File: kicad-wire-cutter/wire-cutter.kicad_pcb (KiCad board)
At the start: 2 copper layers, 60.7 x 113.1 mm, 21 parts, among them J1 Conn_01x01_Socket, J3 Conn_01x01_Socket, U4 ESP32-DEVKIT-V1

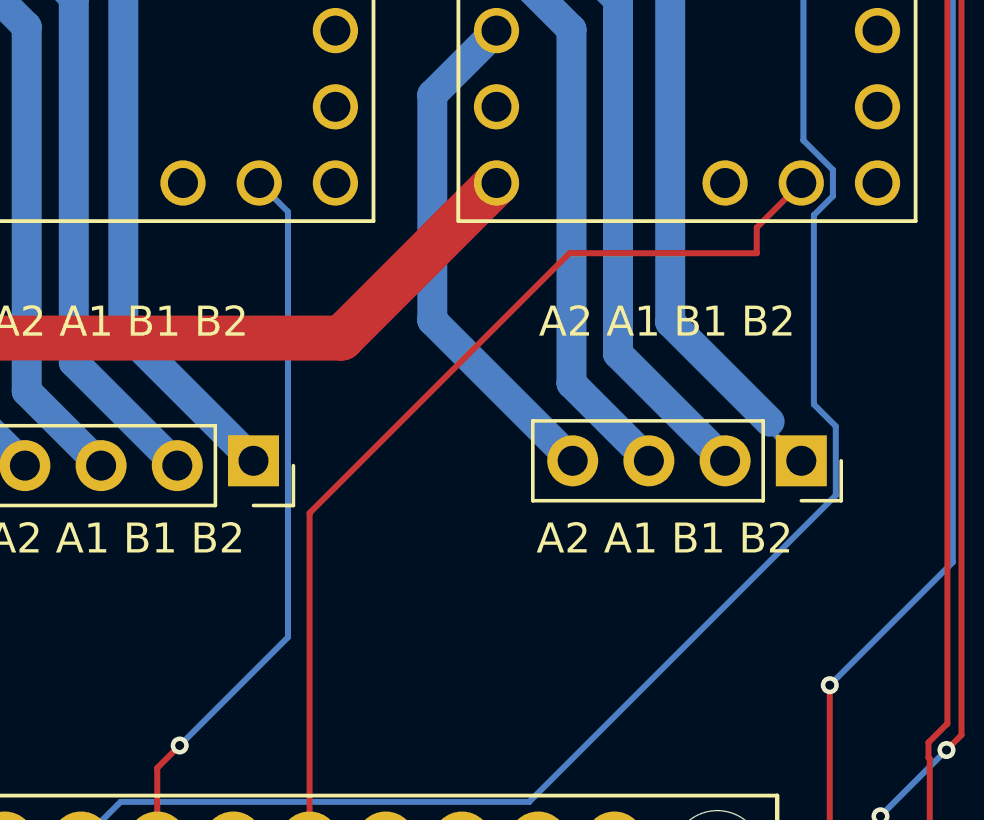
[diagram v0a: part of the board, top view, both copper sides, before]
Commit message: Finished full cut process
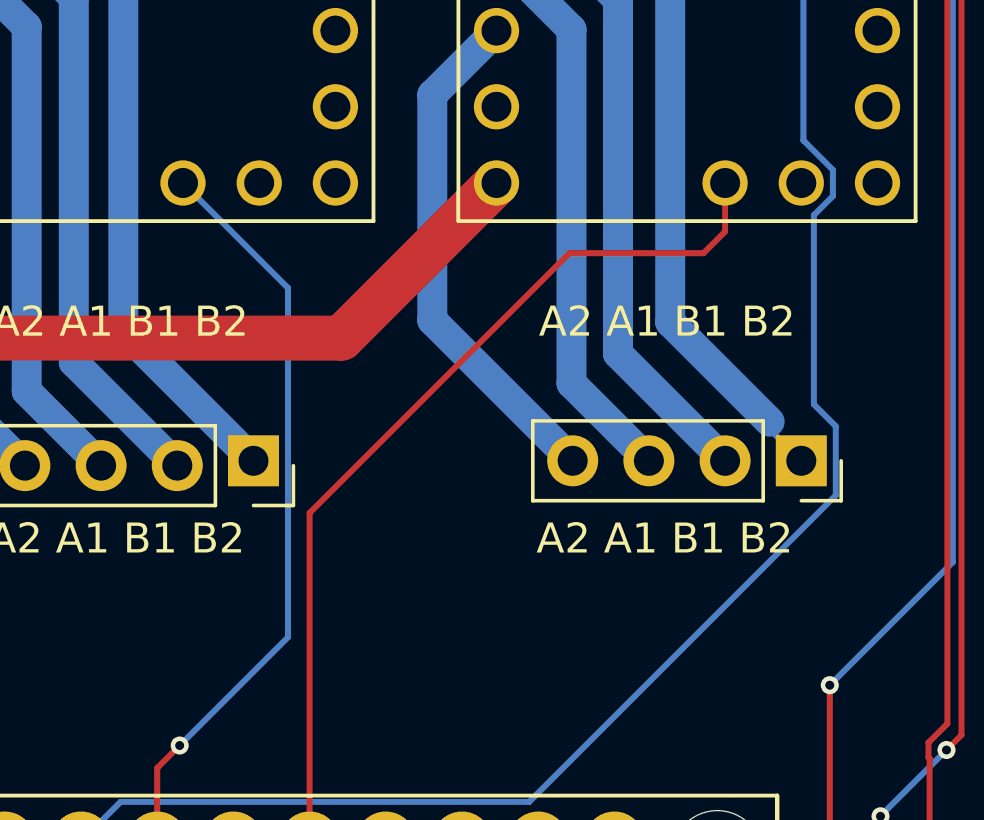
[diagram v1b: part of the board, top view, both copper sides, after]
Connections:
- LINMOT1 pad 17: unconnected-(LINMOT1-INDEX-Pad17) -> Net-(LINMOT1-INDEX)
- LINMOT1 pad 18: Net-(LINMOT1-DIAG) -> unconnected-(LINMOT1-DIAG-Pad18)
- LINMOT2 pad 17: unconnected-(LINMOT2-INDEX-Pad17) -> Net-(LINMOT2-INDEX)
- LINMOT2 pad 18: Net-(LINMOT2-DIAG) -> unconnected-(LINMOT2-DIAG-Pad18)
- U4 pad 20: Net-(LINMOT2-DIAG) -> Net-(LINMOT2-INDEX)
- U4 pad 22: Net-(LINMOT1-DIAG) -> Net-(LINMOT1-INDEX)
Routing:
- net Net-(LINMOT2-DIAG): track 32.4 -> 0.00 mm
- net Net-(LINMOT2-INDEX): track 0.00 -> 30.3 mm
- net Net-(LINMOT1-INDEX): track 0.00 -> 25.2 mm, vias 0 -> 1
- net Net-(LINMOT1-DIAG): track 24.2 -> 0.00 mm, vias 1 -> 0
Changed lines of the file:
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@@
 	(net 19 "Net-(EXTRUDER1-M2A)")
 	(net 20 "unconnected-(LINMOT1-PDN-Pad11)")
-	(net 21 "Net-(LINMOT1-DIAG)")
+	(net 21 "unconnected-(LINMOT1-DIAG-Pad18)")
 	(net 22 "Net-(LINMOT1-STEP)")
 	(net 23 "Net-(LINMOT1-DIR)")
-	(net 24 "unconnected-(LINMOT1-INDEX-Pad17)")
-	(net 25 "unconnected-(LINMOT2-INDEX-Pad17)")
+	(net 24 "Net-(LINMOT1-INDEX)")
+	(net 25 "Net-(LINMOT2-INDEX)")
 	(net 26 "unconnected-(LINMOT2-PDN-Pad11)")
-	(net 27 "Net-(LINMOT2-DIAG)")
+	(net 27 "unconnected-(LINMOT2-DIAG-Pad18)")
 	(net 28 "unconnected-(U4-D4-Pad5)")
 	(net 29 "unconnected-(U4-D34-Pad19)")
@@
 			(layers "*.Cu" "*.Mask")
 			(remove_unused_layers no)
-			(net 27 "Net-(LINMOT2-DIAG)")
+			(net 25 "Net-(LINMOT2-INDEX)")
 			(pinfunction "D35")
 			(pintype "bidirectional")
@@
 			(layers "*.Cu" "*.Mask")
 			(remove_unused_layers no)
-			(net 21 "Net-(LINMOT1-DIAG)")
+			(net 24 "Net-(LINMOT1-INDEX)")
 			(pinfunction "D33")
 			(pintype "bidirectional")
@@
 		)
 		(fp_text user "${REFERENCE}"
-			(at 0 3.81 360)
+			(at 0 3.81 0)
 			(layer "F.Fab")
 			(effects
@@
 			(layers "*.Cu" "*.Mask")
 			(remove_unused_layers no)
-			(net 25 "unconnected-(LINMOT2-INDEX-Pad17)")
+			(net 25 "Net-(LINMOT2-INDEX)")
 			(pinfunction "INDEX")
-			(pintype "output+no_connect")
+			(pintype "output")
 			(solder_mask_margin 0.102)
 		)
@@
 			(layers "*.Cu" "*.Mask")
 			(remove_unused_layers no)
-			(net 27 "Net-(LINMOT2-DIAG)")
+			(net 27 "unconnected-(LINMOT2-DIAG-Pad18)")
 			(pinfunction "DIAG")
-			(pintype "output")
+			(pintype "output+no_connect")
 			(solder_mask_margin 0.102)
 		)
@@
 			(layers "*.Cu" "*.Mask")
 			(remove_unused_layers no)
-			(net 24 "unconnected-(LINMOT1-INDEX-Pad17)")
+			(net 24 "Net-(LINMOT1-INDEX)")
 			(pinfunction "INDEX")
-			(pintype "output+no_connect")
+			(pintype "output")
 			(solder_mask_margin 0.102)
 		)
@@
 			(layers "*.Cu" "*.Mask")
 			(remove_unused_layers no)
-			(net 21 "Net-(LINMOT1-DIAG)")
+			(net 21 "unconnected-(LINMOT1-DIAG-Pad18)")
 			(pinfunction "DIAG")
-			(pintype "output")
+			(pintype "output+no_connect")
 			(solder_mask_margin 0.102)
 		)
@@
 		)
 		(fp_text user "${REFERENCE}"
-			(at 0 3.81 360)
+			(at 0 3.81 0)
 			(layer "F.Fab")
 			(effects
@@
 		(tags "Through hole pin header THT 1x04 2.54mm single row")
 		(property "Reference" "EC11"
-			(at 0 -2.33 360)
+			(at 0 -2.33 0)
 			(layer "F.SilkS")
 			(effects
@@
 	)
 	(segment
-		(start 93.44 71.2)
-		(end 93.44 73.65)
-		(width 0.2)
-		(layer "F.Cu")
-		(net 21)
-	)
-	(segment
-		(start 94.19 70.45)
-		(end 93.44 71.2)
-		(width 0.2)
-		(layer "F.Cu")
-		(net 21)
-	)
-	(via
-		(at 94.19 70.45)
-		(size 0.6)
-		(drill 0.3)
-		(layers "F.Cu" "B.Cu")
-		(net 21)
-	)
-	(segment
-		(start 96.84 51.7)
-		(end 97.8 52.66)
-		(width 0.2)
-		(layer "B.Cu")
-		(net 21)
-	)
-	(segment
-		(start 97.8 66.84)
-		(end 94.19 70.45)
-		(width 0.2)
-		(layer "B.Cu")
-		(net 21)
-	)
-	(segment
-		(start 97.8 52.66)
-		(end 97.8 66.84)
-		(width 0.2)
-		(layer "B.Cu")
-		(net 21)
-	)
-	(segment
 		(start 116.396 37.514)
 		(end 117.45 36.46)
@@
 	)
 	(segment
-		(start 107.18 54.04)
-		(end 98.52 62.7)
+		(start 93.44 71.2)
+		(end 93.44 73.65)
 		(width 0.2)
 		(layer "F.Cu")
-		(net 27)
+		(net 24)
 	)
 	(segment
-		(start 98.52 62.7)
-		(end 98.52 73.65)
+		(start 94.19 70.45)
+		(end 93.44 71.2)
 		(width 0.2)
 		(layer "F.Cu")
-		(net 27)
+		(net 24)
+	)
+	(via
+		(at 94.19 70.45)
+		(size 0.6)
+		(drill 0.3)
+		(layers "F.Cu" "B.Cu")
+		(net 24)
+	)
+	(segment
+		(start 97.8 55.2)
+		(end 97.8 55.45)
+		(width 0.2)
+		(layer "B.Cu")
+		(net 24)
+	)
+	(segment
+		(start 97.8 55.45)
+		(end 97.8 66.84)
+		(width 0.2)
+		(layer "B.Cu")
+		(net 24)
 	)
 	(segment
-		(start 113.424 54.04)
+		(start 94.3 51.7)
+		(end 97.8 55.2)
+		(width 0.2)
+		(layer "B.Cu")
+		(net 24)
+	)
+	(segment
+		(start 97.8 66.84)
+		(end 94.19 70.45)
+		(width 0.2)
+		(layer "B.Cu")
+		(net 24)
+	)
+	(segment
+		(start 111.65 54.04)
 		(end 107.18 54.04)
 		(width 0.2)
 		(layer "F.Cu")
-		(net 27)
+		(net 25)
+	)
+	(segment
+		(start 107.18 54.04)
+		(end 98.52 62.7)
+		(width 0.2)
+		(layer "F.Cu")
+		(net 25)
 	)
 	(segment
-		(start 114.91 51.7)
-		(end 113.424 53.186)
+		(start 112.37 53.32)
+		(end 111.65 54.04)
+		(width 0.2)
+		(layer "F.Cu")
+		(net 25)
+	)
+	(segment
+		(start 98.52 62.7)
+		(end 98.52 73.65)
 		(width 0.2)
 		(layer "F.Cu")
-		(net 27)
+		(net 25)
 	)
 	(segment
-		(start 113.424 53.186)
-		(end 113.424 54.04)
+		(start 112.37 51.7)
+		(end 112.37 53.32)
 		(width 0.2)
 		(layer "F.Cu")
-		(net 27)
+		(net 25)
 	)
 	(segment
